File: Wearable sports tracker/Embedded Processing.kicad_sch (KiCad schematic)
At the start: 7 parts, among them U1 STM32WB55RGVx

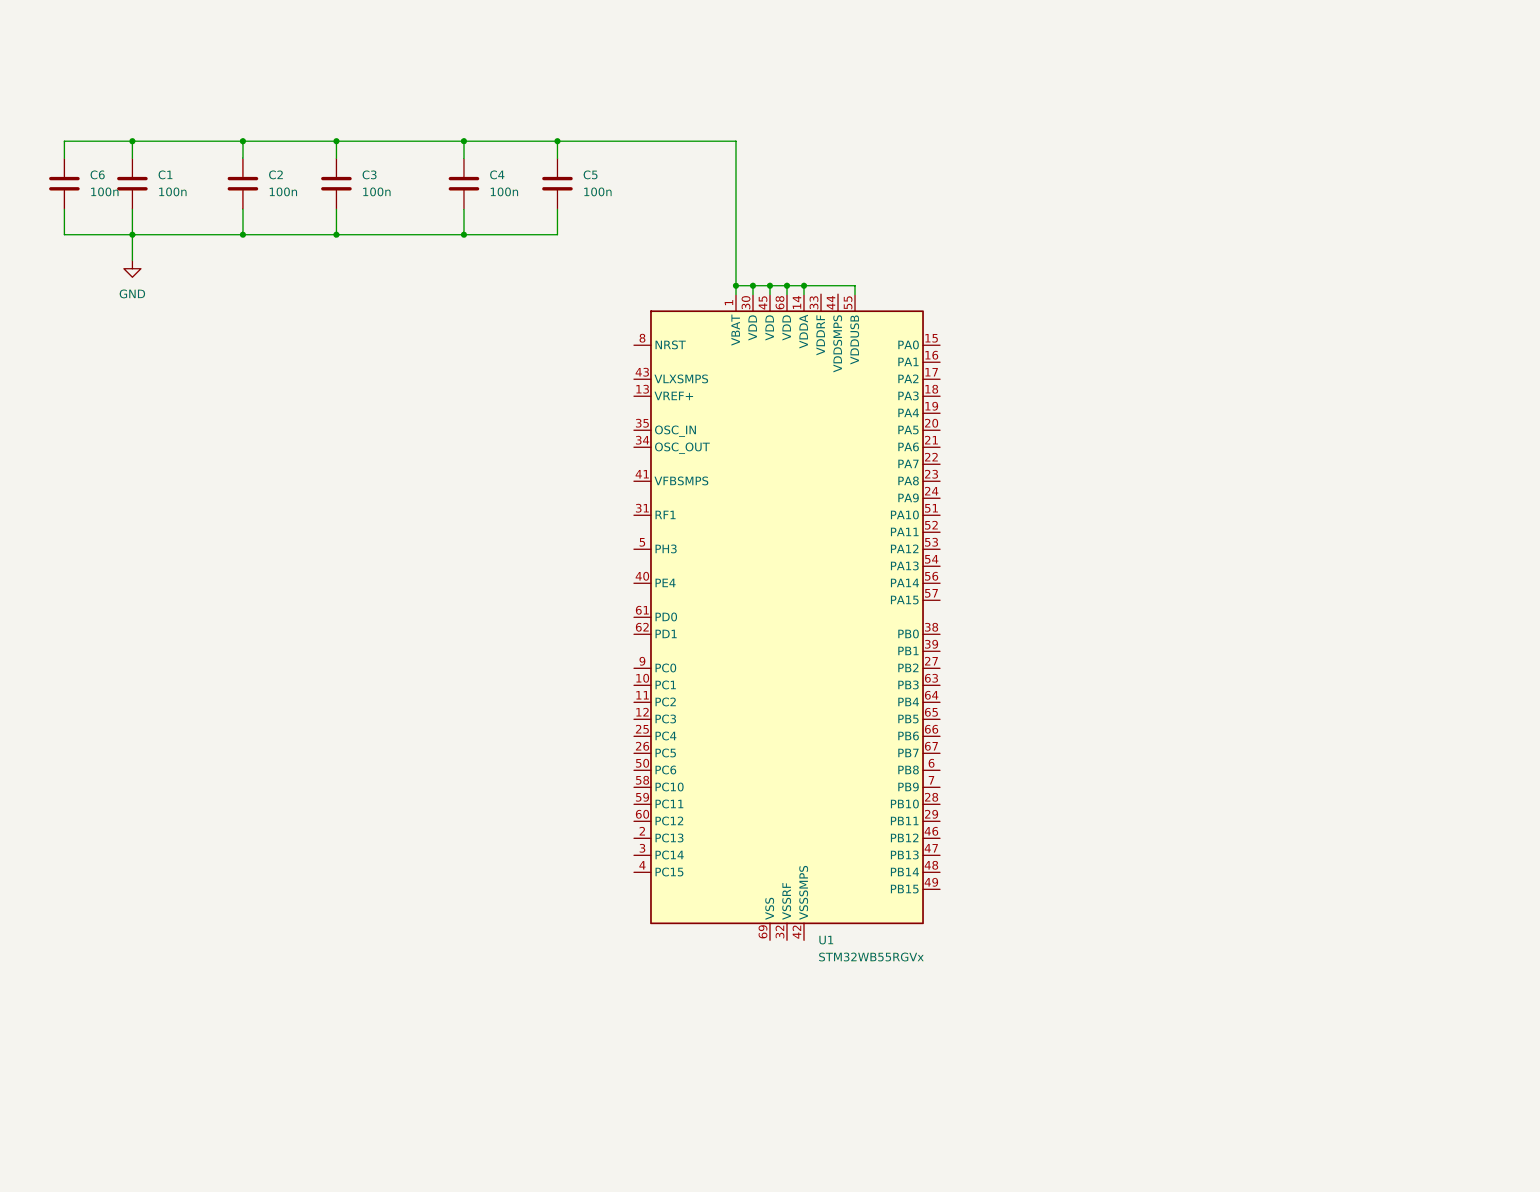
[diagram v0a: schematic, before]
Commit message: MCU HSE & LSE Crystals
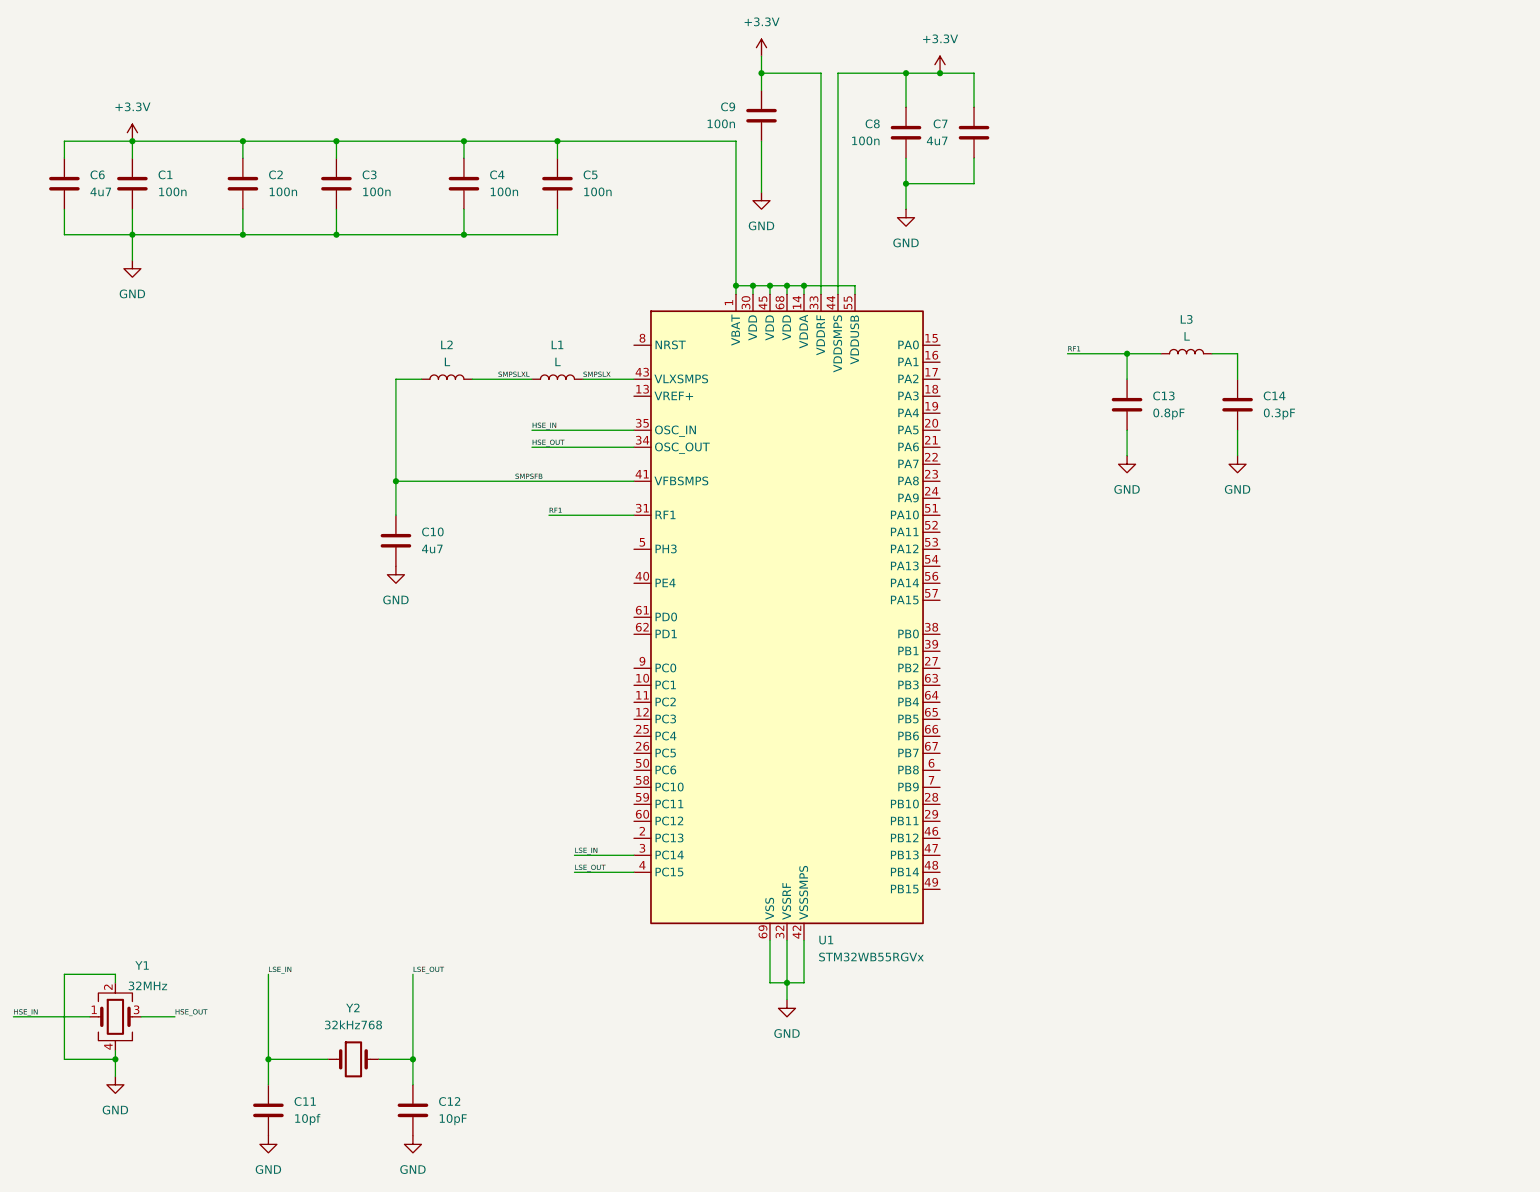
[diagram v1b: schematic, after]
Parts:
- added C10, C7: 4u7, symbol Device:C
- added C11: 10pf, symbol Device:C
- added C12: 10pF, symbol Device:C
- added C13: 0.8pF, symbol Device:C
- added C14: 0.3pF, symbol Device:C
- added C8, C9: 100n, symbol Device:C
- added L1, L2, L3: L, symbol Device:L
- added Y1: 32MHz, symbol Device:Crystal_GND24
- added Y2: 32kHz768, symbol Device:Crystal
- C6: value 100n -> 4u7
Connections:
- net GND: now also U1.32 (VSSRF), U1.42 (VSSSMPS), U1.69 (VSS), C10.2, C11.2, C12.2, C13.2, C14.2, C7.2, C8.2, C9.2, Y1.2, Y1.4
- net +3.3V: now reaches C1.1, C2.1, C3.1, C4.1, C5.1, C6.1, U1.1 (VBAT), U1.14 (VDDA), U1.30 (VDD), U1.45 (VDD), U1.55 (VDDUSB), U1.68 (VDD)
- net +3.3V: now also U1.33 (VDDRF), U1.44 (VDDSMPS), C7.1, C8.1, C9.1
- net LSE_IN: now reaches U1.3 (PC14)
- net LSE_IN: now also C11.1, Y2.1
- net RF1: now reaches U1.31 (RF1)
- net RF1: now also C13.1, L3.1
- net HSE_OUT: now reaches U1.34 (OSC_OUT)
- net HSE_OUT: now also Y1.3
- net HSE_IN: now reaches U1.35 (OSC_IN)
- net HSE_IN: now also Y1.1
- net LSE_OUT: now reaches U1.4 (PC15)
- net LSE_OUT: now also C12.1, Y2.2
- net SMPSFB: now reaches U1.41 (VFBSMPS)
- net SMPSFB: now also C10.1, L2.1
- net SMPSLX: now reaches U1.43 (VLXSMPS)
- net SMPSLX: now also L1.2
- new net: C14.1, L3.2
- new net SMPSLXL: L1.1, L2.2

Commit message: RF section
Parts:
- removed C13: 0.8pF, symbol Device:C
- removed C14: 0.3pF, symbol Device:C
- removed L3: L, symbol Device:L
- added J2: Conn_ARM_SWD_TagConnect_TC2030-NL, Connector:Tag-Connect_TC2030-IDC-NL_2x03_P1.27mm_Vertical, symbol Connector:Conn_ARM_SWD_TagConnect_TC2030-NL

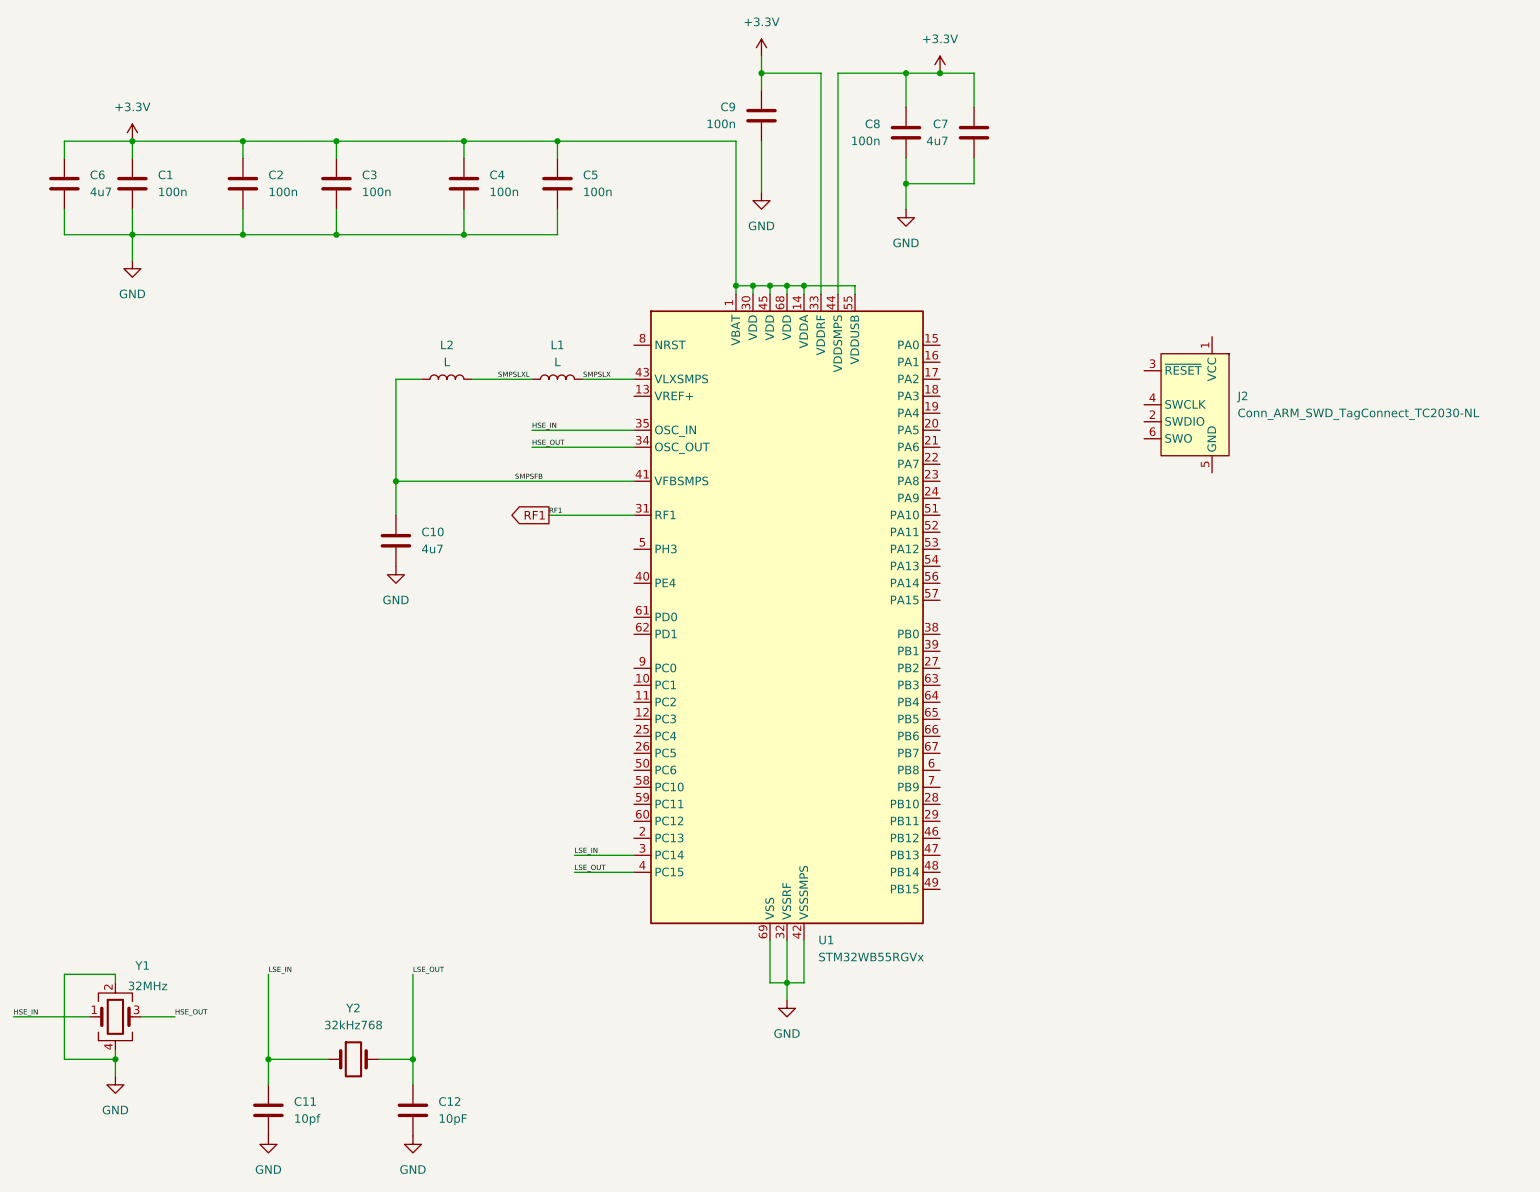
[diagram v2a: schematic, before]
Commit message: Programming Interface (SWD/BOOT)
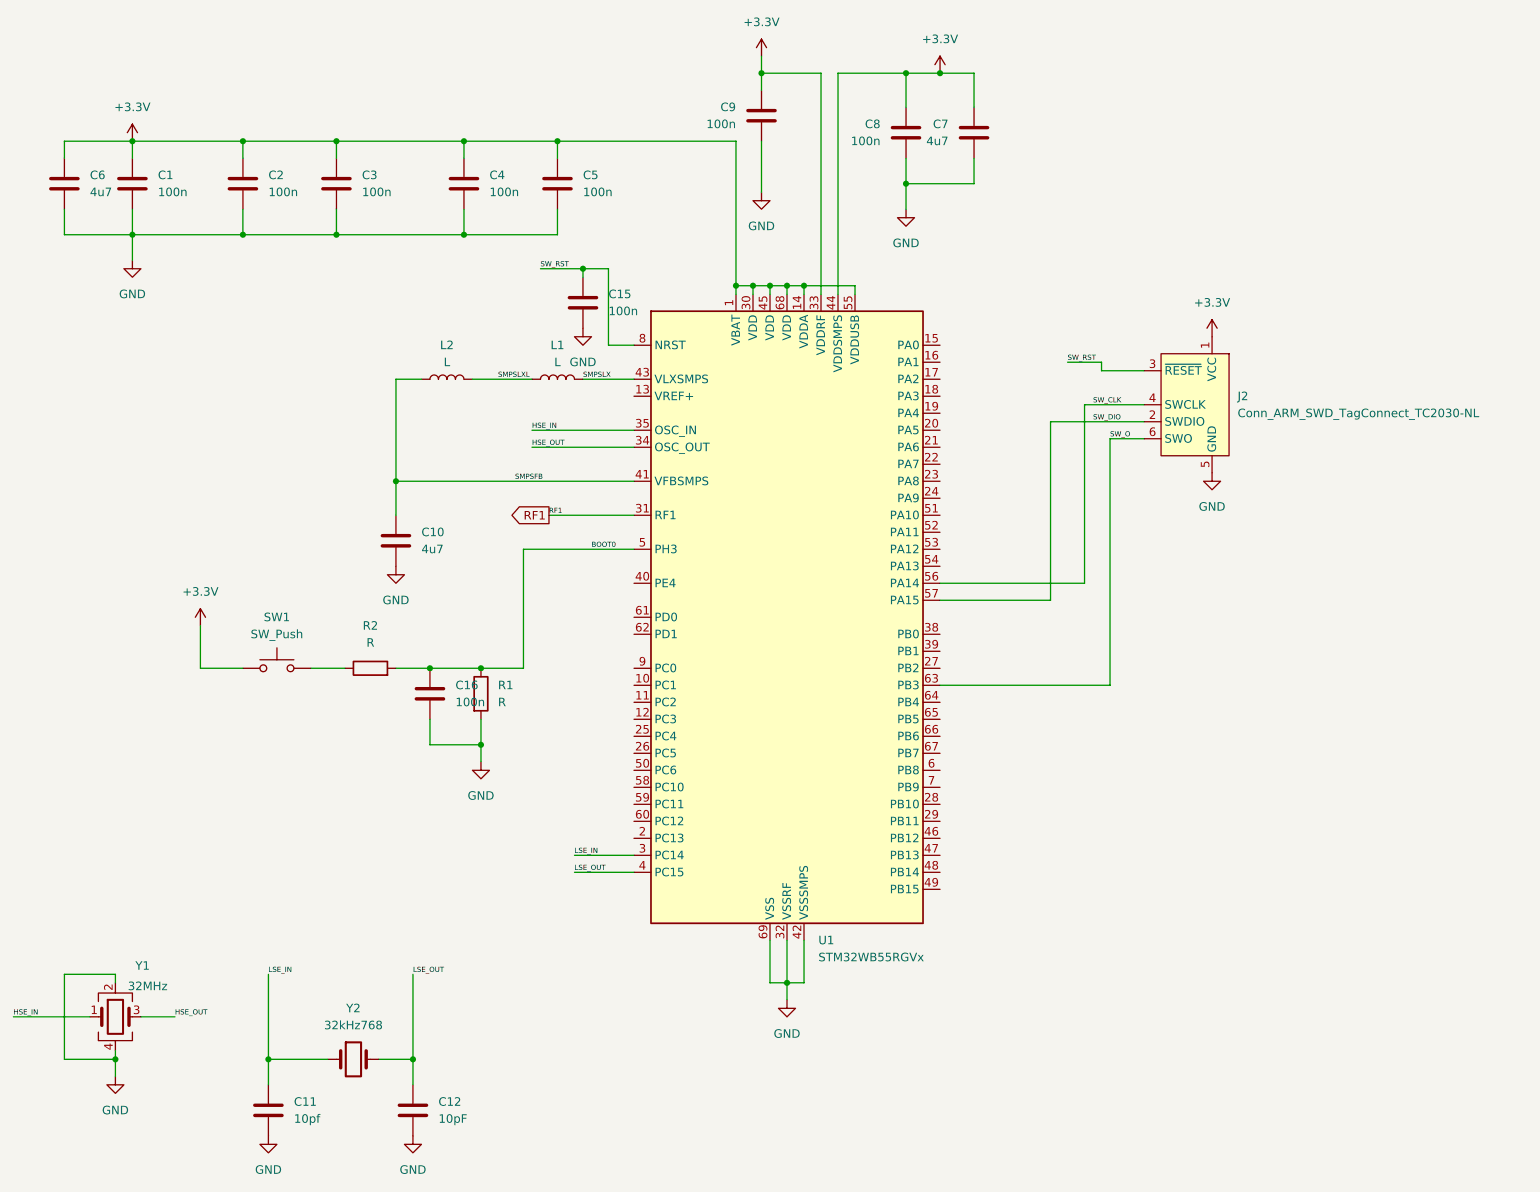
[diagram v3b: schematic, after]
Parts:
- added C15, C16: 100n, symbol Device:C
- added R1, R2: R, symbol Device:R
- added SW1: SW_Push, symbol Switch:SW_Push
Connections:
- net +3.3V: now also J2.1 (VCC), SW1.1
- net GND: now also J2.5 (GND), C15.2, C16.2, R1.2
- net BOOT0: now reaches U1.5 (PH3)
- net BOOT0: now also C16.1, R1.1, R2.2
- net SW_CLK: now reaches U1.56 (PA14)
- net SW_CLK: now also J2.4 (SWCLK)
- net SW_DIO: now reaches U1.57 (PA15)
- net SW_DIO: now also J2.2 (SWDIO)
- net SW_O: now reaches U1.63 (PB3)
- net SW_O: now also J2.6 (SWO)
- net SW_RST: now reaches U1.8 (NRST)
- net SW_RST: now also J2.3 (~{RESET}), C15.1
- new net: R2.1, SW1.2
